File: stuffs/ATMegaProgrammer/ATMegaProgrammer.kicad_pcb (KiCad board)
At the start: 2 copper layers, 27.9 x 47 mm, 4 parts, among them CON1 AVR-ISP-6, IC1 ATMEGA328P-P, P1 CONN_01X14, P2 CONN_01X14

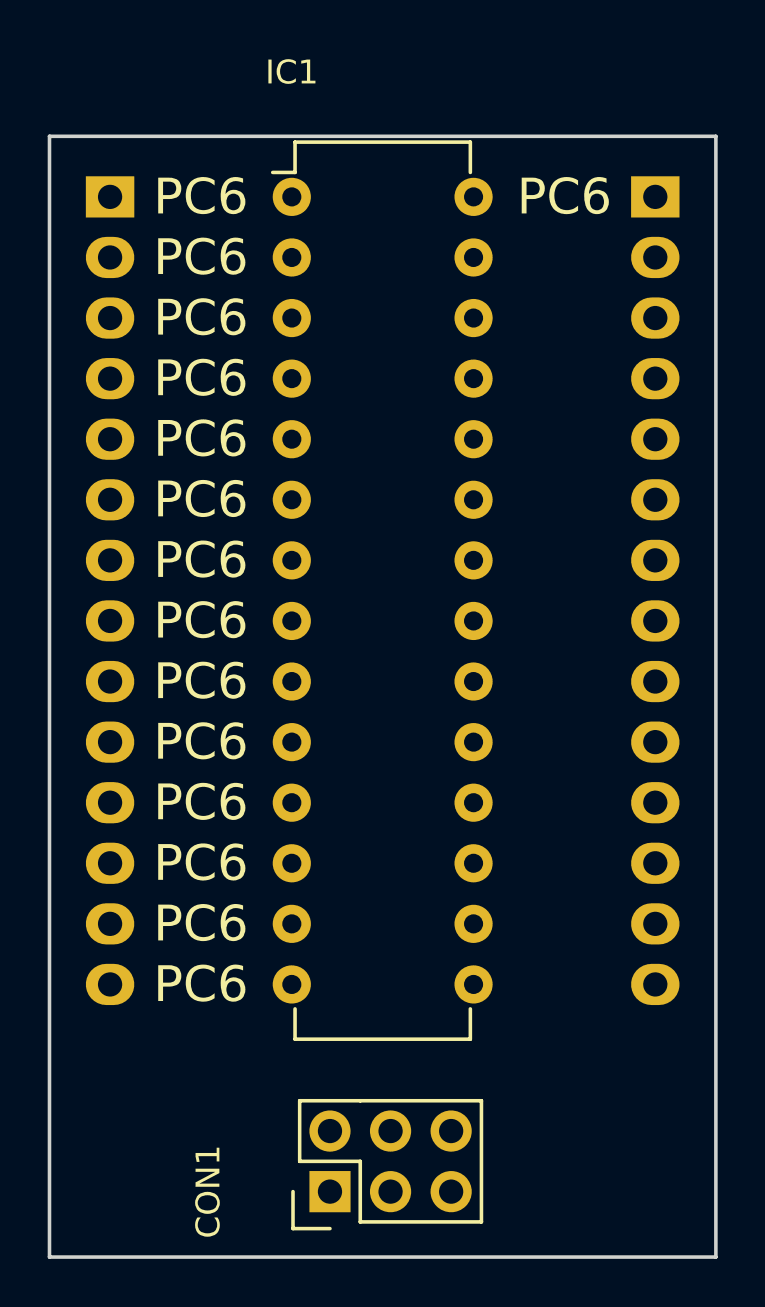
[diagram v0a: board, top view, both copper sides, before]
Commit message: Improve ATMega328Programmer.
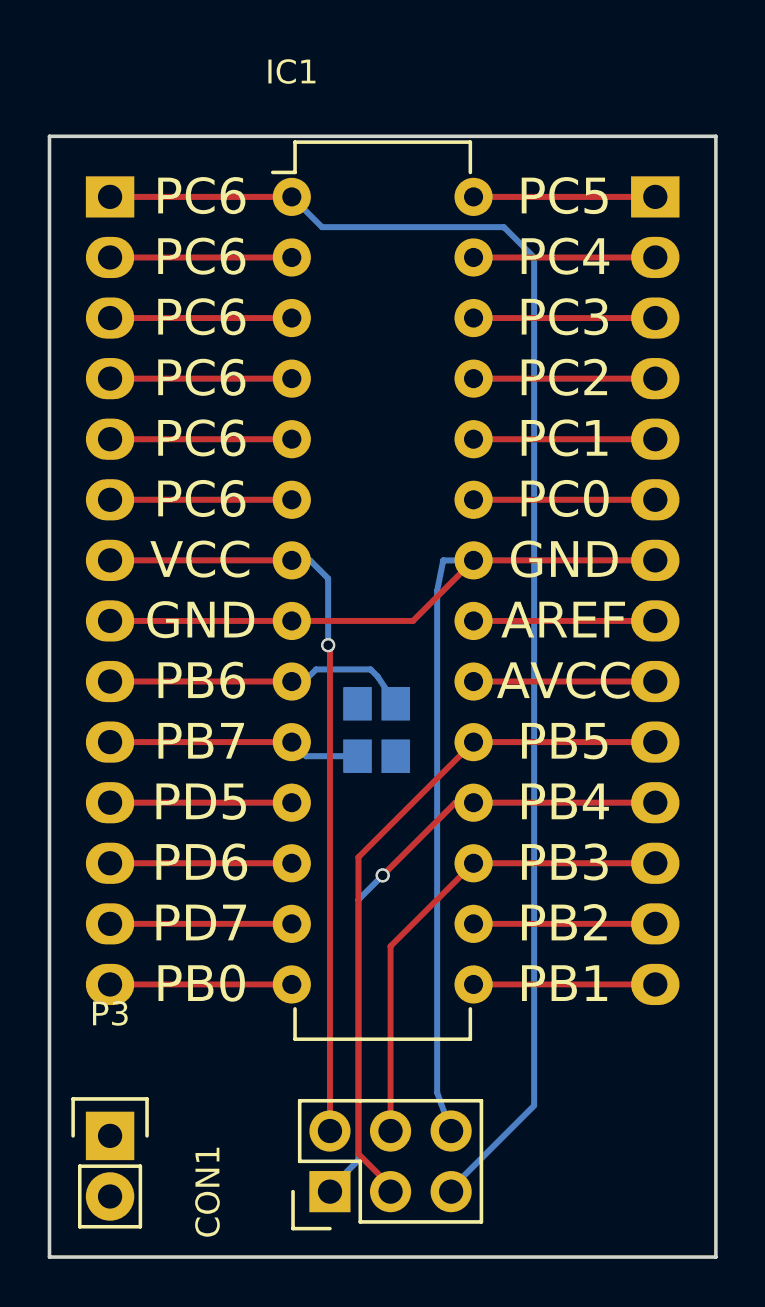
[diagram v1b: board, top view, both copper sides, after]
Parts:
- added P3: CONN_01X02, Pin_Headers:Pin_Header_Straight_1x02, F.Cu at (154.9, 139.7)
- added X1: CRYSTAL_SMD, Crystals:crystal_FA238-TSX3225, B.Cu at (166.1, 122.7)
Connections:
- CON1 pad 1: Net-(CON1-Pad1) -> PB4
- CON1 pad 2: Net-(CON1-Pad2) -> VCC
- CON1 pad 3: Net-(CON1-Pad3) -> PB5
- CON1 pad 4: Net-(CON1-Pad4) -> PB3
- CON1 pad 5: Net-(CON1-Pad5) -> PC6
- CON1 pad 6: Net-(CON1-Pad6) -> GND
- IC1 pad 1: P1 -> PC6
- IC1 pad 10: Net-(IC1-Pad10) -> PB7
- IC1 pad 11: Net-(IC1-Pad11) -> PD5
- IC1 pad 12: Net-(IC1-Pad12) -> PD6
- IC1 pad 13: Net-(IC1-Pad13) -> PD7
- IC1 pad 14: Net-(IC1-Pad14) -> PB0
- IC1 pad 15: Net-(IC1-Pad15) -> PB1
- IC1 pad 16: Net-(IC1-Pad16) -> PB2
- IC1 pad 17: Net-(IC1-Pad17) -> PB3
- IC1 pad 18: Net-(IC1-Pad18) -> PB4
- IC1 pad 19: Net-(IC1-Pad19) -> PB5
- IC1 pad 2: Net-(IC1-Pad2) -> PD0
- IC1 pad 20: Net-(IC1-Pad20) -> AVCC
- IC1 pad 21: Net-(IC1-Pad21) -> AREF
- IC1 pad 22: Net-(IC1-Pad22) -> GND
- IC1 pad 23: Net-(IC1-Pad23) -> PC0
- IC1 pad 24: Net-(IC1-Pad24) -> PC1
- IC1 pad 25: Net-(IC1-Pad25) -> PC2
- IC1 pad 26: Net-(IC1-Pad26) -> PC3
- IC1 pad 27: Net-(IC1-Pad27) -> PC4
- IC1 pad 28: Net-(IC1-Pad28) -> PC5
- IC1 pad 3: Net-(IC1-Pad3) -> PD1
- IC1 pad 4: Net-(IC1-Pad4) -> PD2
- IC1 pad 5: Net-(IC1-Pad5) -> PD3
- IC1 pad 6: Net-(IC1-Pad6) -> PD4
- IC1 pad 7: Net-(IC1-Pad7) -> VCC
- IC1 pad 8: Net-(IC1-Pad8) -> GND
- IC1 pad 9: Net-(IC1-Pad9) -> PB6
- P1 pad 1: P1 -> PC6
- P1 pad 10: Net-(P1-Pad10) -> PB7
- P1 pad 11: Net-(P1-Pad11) -> PD5
- P1 pad 12: Net-(P1-Pad12) -> PD6
- P1 pad 13: Net-(P1-Pad13) -> PD7
- P1 pad 14: Net-(P1-Pad14) -> PB0
- P1 pad 2: Net-(P1-Pad2) -> PD0
- P1 pad 3: Net-(P1-Pad3) -> PD1
- P1 pad 4: Net-(P1-Pad4) -> PD2
- P1 pad 5: Net-(P1-Pad5) -> PD3
- P1 pad 6: Net-(P1-Pad6) -> PD4
- P1 pad 7: Net-(P1-Pad7) -> VCC
- P1 pad 8: Net-(P1-Pad8) -> GND
- P1 pad 9: Net-(P1-Pad9) -> PB6
- P2 pad 1: Net-(P2-Pad1) -> PC5
- P2 pad 10: Net-(P2-Pad10) -> PB5
- P2 pad 11: Net-(P2-Pad11) -> PB4
- P2 pad 12: Net-(P2-Pad12) -> PB3
- P2 pad 13: Net-(P2-Pad13) -> PB2
- P2 pad 14: Net-(P2-Pad14) -> PB1
- P2 pad 2: Net-(P2-Pad2) -> PC4
- P2 pad 3: Net-(P2-Pad3) -> PC3
- P2 pad 4: Net-(P2-Pad4) -> PC2
- P2 pad 5: Net-(P2-Pad5) -> PC1
- P2 pad 6: Net-(P2-Pad6) -> PC0
- P2 pad 7: Net-(P2-Pad7) -> GND
- P2 pad 8: Net-(P2-Pad8) -> AREF
- P2 pad 9: Net-(P2-Pad9) -> AVCC
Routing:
- net PC6: track 0.00 -> 59.4 mm
- net GND: track 0.00 -> 49.2 mm
- net VCC: track 0.00 -> 32.7 mm, vias 0 -> 1
- net PB5: track 0.00 -> 29.0 mm
- net PB4: track 0.00 -> 26.9 mm, vias 0 -> 1
- net PB3: track 0.00 -> 20.3 mm
- net PB6: track 0.00 -> 12.9 mm
- net PB7: track 0.00 -> 10.6 mm
- net PD7: track 0.00 -> 7.62 mm
- net PD6: track 0.00 -> 7.62 mm
- net PD5: track 0.00 -> 7.62 mm
- net PD4: track 0.00 -> 7.62 mm
- net PD3: track 0.00 -> 7.62 mm
- net PD2: track 0.00 -> 7.62 mm
- net PD1: track 0.00 -> 7.62 mm
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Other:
- board text added: "AREF"
- board text added: "AVCC"
- board text added: "GND"
- board text added: "PB0"
- board text added: "PB1"
- board text added: "PB2"
- board text added: "PB3"
- board text added: "PB4"
- board text added: "PB5"
- board text added: "PB6"
- board text added: "PB7"
- board text added: "PC0"
- board text added: "PC1"
- board text added: "PC2"
- board text added: "PC3"
- board text added: "PC4"
- board text added: "PC5"
- board text added: "PD5"
- board text added: "PD6"
- board text added: "PD7"
- board text added: "VCC"

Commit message: Add ground planes, fix labels and connect GND for crystal.
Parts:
- moved P3 0.36 mm to (155.2, 140.0)
- moved P1 0.36 mm to (155.2, 100.6)
- moved P2 0.36 mm to (178.1, 100.6)
- moved X1 0.36 mm to (166.4, 122.9)
- moved CON1 0.36 mm to (164.4, 142.3)
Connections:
- X1 pad 3: Net-(X1-Pad3) -> GND
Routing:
- net GND: track 49.2 -> 0.00 mm
- net VCC: track 32.7 -> 42.2 mm
- net PB6: track 12.9 -> 14.0 mm, vias 0 -> 1
- added copper zone on B.Cu, net GND
- added copper zone on F.Cu, net GND
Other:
- board text added: "PD0"
- board text added: "PD1"
- board text added: "PD2"
- board text added: "PD3"
- board text added: "PD4"
